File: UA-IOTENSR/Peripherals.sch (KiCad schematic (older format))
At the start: 3 parts, among them IC301 LM3914VX_NOPB, U301 SCD4X

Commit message: updated symbols; changed vdd to 3v3 global for pcb design later
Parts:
- DS1: renamed from DS301; symbol Samacs:HDSP-4832 -> UA-IOTENSR-rescue:HDSP-4832-Samacs
- IC1: renamed from IC301; symbol Samacs:LM3914VX_NOPB -> UA-IOTENSR-rescue:LM3914VX_NOPB-Samacs
- renumbered U301 to U4
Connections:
- net labels added: +3V3
- net labels removed: VDD
- wire segments 12 -> 35
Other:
- note added: "PERIPHERALS"
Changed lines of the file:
@@
 P 5750 1450
 AR Path="/61A2D97B" Ref="U?"  Part="1"
-AR Path="/61A1DC3C/61A2D97B" Ref="U301"  Part="1"
-F 0 "U301" H 5750 1915 50  0000 C CNN
+AR Path="/61A1DC3C/61A2D97B" Ref="U4"  Part="1"
+F 0 "U4" H 5750 1915 50  0000 C CNN
 F 1 "SCD4X" H 5750 1824 50  0000 C CNN
 F 2 "" H 5750 1900 50  0001 C CNN
@@
 P 5750 1950
 AR Path="/61A2D98B" Ref="#PWR?"  Part="1"
-AR Path="/61A1DC3C/61A2D98B" Ref="#PWR0302"  Part="1"
-F 0 "#PWR0302" H 5750 1700 50  0001 C CNN
+AR Path="/61A1DC3C/61A2D98B" Ref="#PWR022"  Part="1"
+F 0 "#PWR022" H 5750 1700 50  0001 C CNN
 F 1 "GND" H 5755 1777 50  0000 C CNN
 F 2 "" H 5750 1950 50  0001 C CNN
@@
 Wire Wire Line
 	5300 1400 5100 1400
-Text GLabel 5100 1400 0    50   Input ~ 0
-VDD
 Wire Wire Line
 	5300 1500 5300 1400
 Connection ~ 5300 1400
 $Comp
-L Samacs:HDSP-4832 DS?
+L UA-IOTENSR-rescue:HDSP-4832-Samacs DS?
 U 1 1 61A2D99B
-P 7400 4450
+P 7500 5300
 AR Path="/61A2D99B" Ref="DS?"  Part="1"
-AR Path="/61A1DC3C/61A2D99B" Ref="DS301"  Part="1"
-F 0 "DS301" H 8200 4715 50  0000 C CNN
-F 1 "HDSP-4832" H 8200 4624 50  0000 C CNN
-F 2 "DIPS762W61P254L2540H635Q20N" H 8850 4550 50  0001 L CNN
-F 3 "https://datasheet.datasheetarchive.com/originals/distributors/Datasheets-6/DSA-115790.pdf" H 8850 4450 50  0001 L CNN
-F 4 "Avago Light Bar Array Green/Red/Yellow LED Display, 1900 (Green) ??cd, 1900 (Yellow) ??cd, 3500 (Red) ??cd" H 8850 4350 50  0001 L CNN "Description"
-F 5 "6.35" H 8850 4250 50  0001 L CNN "Height"
-F 6 "630-HDSP-4832" H 8850 4150 50  0001 L CNN "Mouser Part Number"
-F 7 "https://www.mouser.co.uk/ProductDetail/Broadcom-Avago/HDSP-4832?qs=pQfy5%252BKCabLkjNEFwaYNQw%3D%3D" H 8850 4050 50  0001 L CNN "Mouser Price/Stock"
-F 8 "Avago Technologies" H 8850 3950 50  0001 L CNN "Manufacturer_Name"
-F 9 "HDSP-4832" H 8850 3850 50  0001 L CNN "Manufacturer_Part_Number"
-	1    7400 4450
+AR Path="/61A1DC3C/61A2D99B" Ref="DS1"  Part="1"
+F 0 "DS1" H 8300 5565 50  0000 C CNN
+F 1 "HDSP-4832" H 8300 5474 50  0000 C CNN
+F 2 "DIPS762W61P254L2540H635Q20N" H 8950 5400 50  0001 L CNN
+F 3 "https://datasheet.datasheetarchive.com/originals/distributors/Datasheets-6/DSA-115790.pdf" H 8950 5300 50  0001 L CNN
+F 4 "Avago Light Bar Array Green/Red/Yellow LED Display, 1900 (Green) ??cd, 1900 (Yellow) ??cd, 3500 (Red) ??cd" H 8950 5200 50  0001 L CNN "Description"
+F 5 "6.35" H 8950 5100 50  0001 L CNN "Height"
+F 6 "630-HDSP-4832" H 8950 5000 50  0001 L CNN "Mouser Part Number"
+F 7 "https://www.mouser.co.uk/ProductDetail/Broadcom-Avago/HDSP-4832?qs=pQfy5%252BKCabLkjNEFwaYNQw%3D%3D" H 8950 4900 50  0001 L CNN "Mouser Price/Stock"
+F 8 "Avago Technologies" H 8950 4800 50  0001 L CNN "Manufacturer_Name"
+F 9 "HDSP-4832" H 8950 4700 50  0001 L CNN "Manufacturer_Part_Number"
+	1    7500 5300
+	-1   0    0    1
+$EndComp
+Wire Wire Line
+	3000 4650 2800 4650
+$Comp
+L power:GND #PWR?
+U 1 1 61A2D9AF
+P 4100 3650
+AR Path="/61A2D9AF" Ref="#PWR?"  Part="1"
+AR Path="/61A1DC3C/61A2D9AF" Ref="#PWR021"  Part="1"
+F 0 "#PWR021" H 4100 3400 50  0001 C CNN
+F 1 "GND" H 4105 3477 50  0000 C CNN
+F 2 "" H 4100 3650 50  0001 C CNN
+F 3 "" H 4100 3650 50  0001 C CNN
+	1    4100 3650
+	-1   0    0    1
+$EndComp
+NoConn ~ 3000 5250
+Text Notes 7050 7000 0    236  ~ 0
+PERIPHERALS
+Wire Wire Line
+	5000 4400 5900 4400
+Wire Wire Line
+	5000 4500 5900 4500
+Wire Wire Line
+	5000 4600 5900 4600
+Wire Wire Line
+	5000 4700 5900 4700
+Wire Wire Line
+	5000 4800 5900 4800
+Wire Wire Line
+	5000 4900 5900 4900
+Wire Wire Line
+	5000 5000 5900 5000
+Wire Wire Line
+	5000 5100 5900 5100
+Wire Wire Line
+	5900 5200 5000 5200
+Wire Wire Line
+	5000 5300 5900 5300
+Wire Wire Line
+	7500 5300 7500 5200
+Connection ~ 7500 4500
+Wire Wire Line
+	7500 4500 7500 4400
+Connection ~ 7500 4600
+Wire Wire Line
+	7500 4600 7500 4500
+Connection ~ 7500 4700
+Wire Wire Line
+	7500 4700 7500 4600
+Connection ~ 7500 4800
+Wire Wire Line
+	7500 4800 7500 4700
+Connection ~ 7500 4900
+Wire Wire Line
+	7500 4900 7500 4800
+Connection ~ 7500 5000
+Wire Wire Line
+	7500 5000 7500 4900
+Connection ~ 7500 5100
+Wire Wire Line
+	7500 5100 7500 5000
+Connection ~ 7500 5200
+Wire Wire Line
+	7500 5200 7500 5100
+Wire Wire Line
+	7500 4400 7500 4150
+Connection ~ 7500 4400
+Wire Wire Line
+	3900 3850 3900 3700
+Wire Wire Line
+	4100 3850 4100 3650
+Wire Wire Line
+	4000 3850 4000 3700
+Wire Wire Line
+	4000 3700 3900 3700
+Connection ~ 3900 3700
+Wire Wire Line
+	3900 3700 3900 3650
+NoConn ~ 3000 5150
+$Comp
+L power:+3V3 #PWR?
+U 1 1 61A1C945
+P 5100 1400
+F 0 "#PWR?" H 5100 1250 50  0001 C CNN
+F 1 "+3V3" H 5115 1573 50  0000 C CNN
+F 2 "" H 5100 1400 50  0001 C CNN
+F 3 "" H 5100 1400 50  0001 C CNN
+	1    5100 1400
 	1    0    0    -1
 $EndComp
 $Comp
-L Samacs:LM3914VX_NOPB IC?
-U 1 1 61A2D9A7
-P 2750 4600
-AR Path="/61A2D9A7" Ref="IC?"  Part="1"
-AR Path="/61A1DC3C/61A2D9A7" Ref="IC301"  Part="1"
-F 0 "IC301" H 4794 4296 50  0000 L CNN
-F 1 "LM3914VX_NOPB" H 4794 4205 50  0000 L CNN
-F 2 "PLCC127P990X990X457-20N" H 4600 5100 50  0001 L CNN
-F 3 "http://www.ti.com/lit/gpn/lm3914" H 4600 5000 50  0001 L CNN
-F 4 "Dot/Bar Display Driver" H 4600 4900 50  0001 L CNN "Description"
-F 5 "4.57" H 4600 4800 50  0001 L CNN "Height"
-F 6 "926-LM3914VX/NOPB" H 4600 4700 50  0001 L CNN "Mouser Part Number"
-F 7 "https://www.mouser.co.uk/ProductDetail/Texas-Instruments/LM3914VX-NOPB?qs=QbsRYf82W3FGYq5LQoAqbA%3D%3D" H 4600 4600 50  0001 L CNN "Mouser Price/Stock"
-F 8 "Texas Instruments" H 4600 4500 50  0001 L CNN "Manufacturer_Name"
-F 9 "LM3914VX/NOPB" H 4600 4400 50  0001 L CNN "Manufacturer_Part_Number"
-	1    2750 4600
+L power:+3V3 #PWR?
+U 1 1 61A1E13D
+P 3900 3650
+F 0 "#PWR?" H 3900 3500 50  0001 C CNN
+F 1 "+3V3" H 3915 3823 50  0000 C CNN
+F 2 "" H 3900 3650 50  0001 C CNN
+F 3 "" H 3900 3650 50  0001 C CNN
+	1    3900 3650
 	1    0    0    -1
 $EndComp
-NoConn ~ 3550 6000
-NoConn ~ 2750 4900
 $Comp
-L power:GND #PWR?
-U 1 1 61A2D9AF
-P 3650 3700
-AR Path="/61A2D9AF" Ref="#PWR?"  Part="1"
-AR Path="/61A1DC3C/61A2D9AF" Ref="#PWR0301"  Part="1"
-F 0 "#PWR0301" H 3650 3450 50  0001 C CNN
-F 1 "GND" H 3655 3527 50  0000 C CNN
-F 2 "" H 3650 3700 50  0001 C CNN
-F 3 "" H 3650 3700 50  0001 C CNN
-	1    3650 3700
-	-1   0    0    1
+L power:+3V3 #PWR?
+U 1 1 61A1F555
+P 7500 4150
+F 0 "#PWR?" H 7500 4000 50  0001 C CNN
+F 1 "+3V3" H 7515 4323 50  0000 C CNN
+F 2 "" H 7500 4150 50  0001 C CNN
+F 3 "" H 7500 4150 50  0001 C CNN
+	1    7500 4150
+	1    0    0    -1
 $EndComp
-Wire Wire Line
-	3650 3900 3650 3700
-Wire Wire Line
-	3550 3900 3550 3800
-Text GLabel 3550 3800 0    50   Input ~ 0
-VDD
-Wire Wire Line
-	2750 4700 2550 4700
+$Comp
+L UA-IOTENSR-rescue:LM3914VX_NOPB-Samacs IC?
+U 1 1 61A2D9A7
+P 3000 4550
+AR Path="/61A2D9A7" Ref="IC?"  Part="1"
+AR Path="/61A1DC3C/61A2D9A7" Ref="IC1"  Part="1"
+F 0 "IC1" H 3250 3300 50  0000 C CNN
+F 1 "LM3914VX_NOPB" H 3500 3200 50  0000 C CNN
+F 2 "PLCC127P990X990X457-20N" H 4850 5050 50  0001 L CNN
+F 3 "http://www.ti.com/lit/gpn/lm3914" H 4850 4950 50  0001 L CNN
+F 4 "Dot/Bar Display Driver" H 4850 4850 50  0001 L CNN "Description"
+F 5 "4.57" H 4850 4750 50  0001 L CNN "Height"
+F 6 "926-LM3914VX/NOPB" H 4850 4650 50  0001 L CNN "Mouser Part Number"
+F 7 "https://www.mouser.co.uk/ProductDetail/Texas-Instruments/LM3914VX-NOPB?qs=QbsRYf82W3FGYq5LQoAqbA%3D%3D" H 4850 4550 50  0001 L CNN "Mouser Price/Stock"
+F 8 "Texas Instruments" H 4850 4450 50  0001 L CNN "Manufacturer_Name"
+F 9 "LM3914VX/NOPB" H 4850 4350 50  0001 L CNN "Manufacturer_Part_Number"
+	1    3000 4550
+	1    0    0    -1
+$EndComp
 $EndSCHEMATC

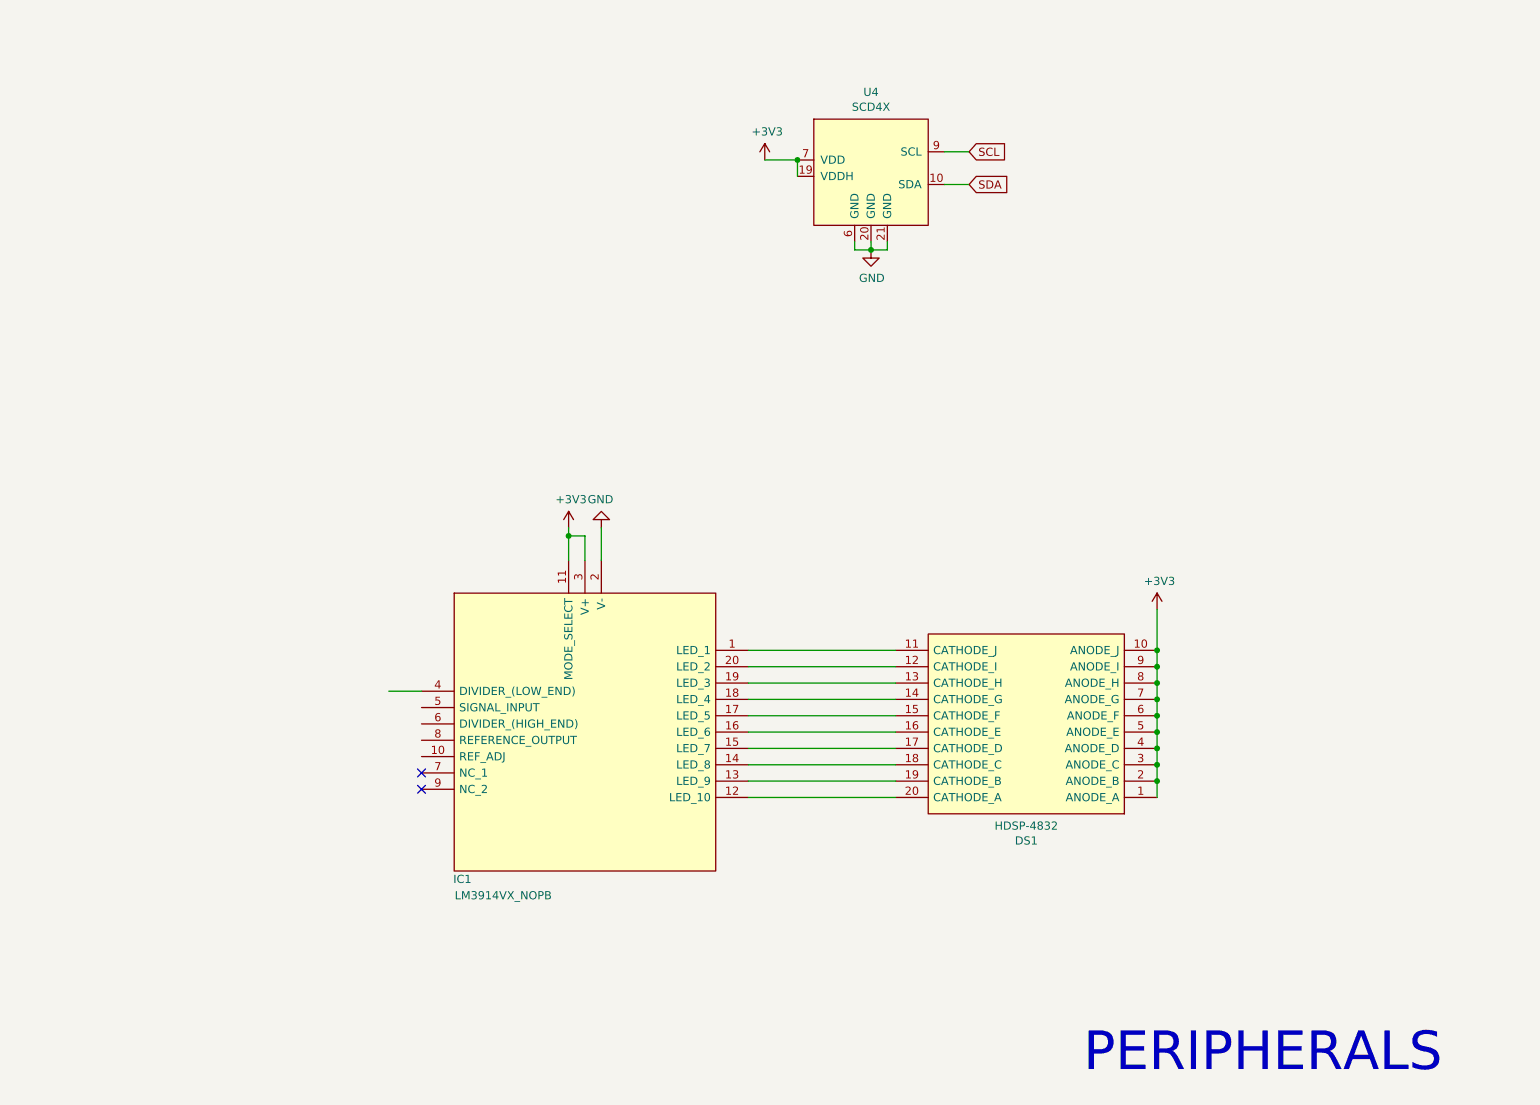
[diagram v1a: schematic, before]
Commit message: Finished LED bar graph array schem
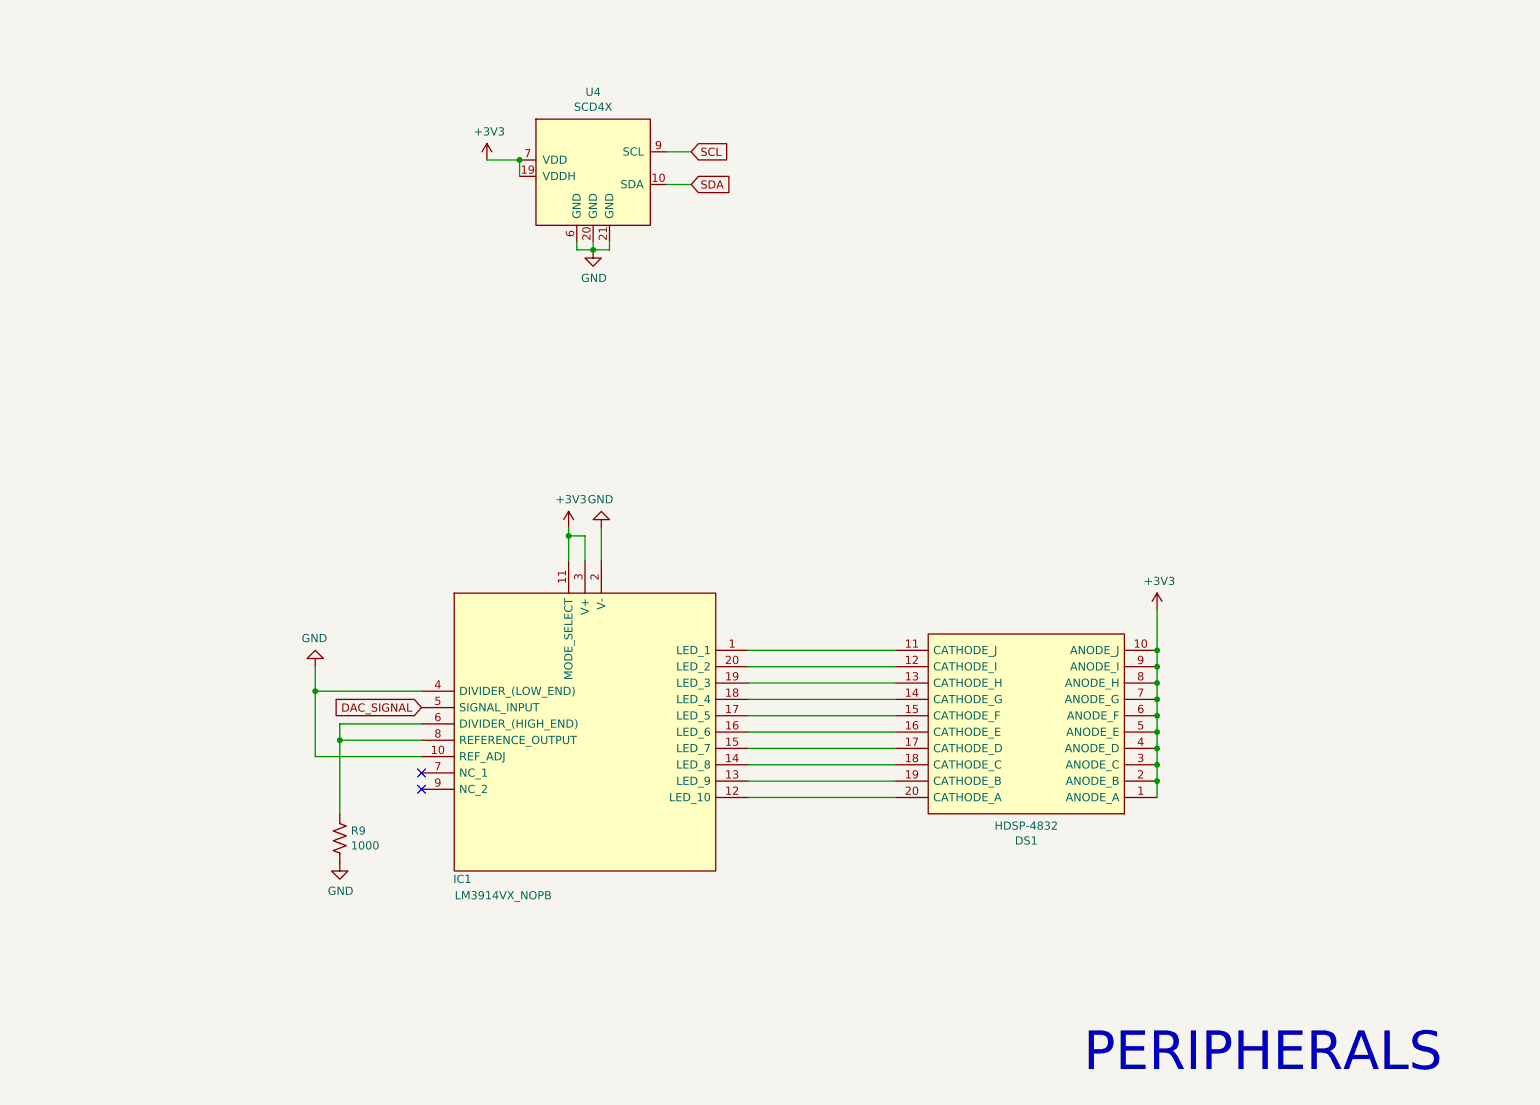
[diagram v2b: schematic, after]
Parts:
- added R9: 1000, symbol Device:R_US
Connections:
- net GND: now also IC1.10 (REF_ADJ), IC1.4 (DIVIDER_(LOW_END)), R9.2
- net DAC_SIGNAL: now reaches IC1.5 (SIGNAL_INPUT)
- net at IC1.6 (DIVIDER_(HIGH_END)): now also IC1.8 (REFERENCE_OUTPUT), R9.1
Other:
- moved on the sheet: U4
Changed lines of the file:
@@
 L SCD4X:SCD4X U?
 U 1 1 61A2D97B
-P 5750 1450
+P 4050 1450
 AR Path="/61A2D97B" Ref="U?"  Part="1"
 AR Path="/61A1DC3C/61A2D97B" Ref="U4"  Part="1"
-F 0 "U4" H 5750 1915 50  0000 C CNN
-F 1 "SCD4X" H 5750 1824 50  0000 C CNN
-F 2 "" H 5750 1900 50  0001 C CNN
-F 3 "" H 5750 1900 50  0001 C CNN
-	1    5750 1450
-	1    0    0    -1
-$EndComp
-Wire Wire Line
-	6200 1350 6350 1350
-Wire Wire Line
-	6200 1550 6350 1550
-Text GLabel 6350 1350 2    50   Input ~ 0
+F 0 "U4" H 4050 1915 50  0000 C CNN
+F 1 "SCD4X" H 4050 1824 50  0000 C CNN
+F 2 "" H 4050 1900 50  0001 C CNN
+F 3 "" H 4050 1900 50  0001 C CNN
+	1    4050 1450
+	1    0    0    -1
+$EndComp
+Wire Wire Line
+	4500 1350 4650 1350
+Wire Wire Line
+	4500 1550 4650 1550
+Text GLabel 4650 1350 2    50   Input ~ 0
 SCL
-Text GLabel 6350 1550 2    50   Input ~ 0
+Text GLabel 4650 1550 2    50   Input ~ 0
 SDA
 Wire Wire Line
-	5650 1900 5650 1950
-Wire Wire Line
-	5650 1950 5750 1950
-Wire Wire Line
-	5850 1950 5850 1900
-Wire Wire Line
-	5750 1900 5750 1950
-Connection ~ 5750 1950
-Wire Wire Line
-	5750 1950 5850 1950
+	3950 1900 3950 1950
+Wire Wire Line
+	3950 1950 4050 1950
+Wire Wire Line
+	4150 1950 4150 1900
+Wire Wire Line
+	4050 1900 4050 1950
+Connection ~ 4050 1950
+Wire Wire Line
+	4050 1950 4150 1950
 $Comp
 L power:GND #PWR?
 U 1 1 61A2D98B
-P 5750 1950
+P 4050 1950
 AR Path="/61A2D98B" Ref="#PWR?"  Part="1"
 AR Path="/61A1DC3C/61A2D98B" Ref="#PWR022"  Part="1"
-F 0 "#PWR022" H 5750 1700 50  0001 C CNN
-F 1 "GND" H 5755 1777 50  0000 C CNN
-F 2 "" H 5750 1950 50  0001 C CNN
-F 3 "" H 5750 1950 50  0001 C CNN
-	1    5750 1950
-	1    0    0    -1
-$EndComp
-Wire Wire Line
-	5300 1400 5100 1400
-Wire Wire Line
-	5300 1500 5300 1400
-Connection ~ 5300 1400
+F 0 "#PWR022" H 4050 1700 50  0001 C CNN
+F 1 "GND" H 4055 1777 50  0000 C CNN
+F 2 "" H 4050 1950 50  0001 C CNN
+F 3 "" H 4050 1950 50  0001 C CNN
+	1    4050 1950
+	1    0    0    -1
+$EndComp
+Wire Wire Line
+	3600 1400 3400 1400
+Wire Wire Line
+	3600 1500 3600 1400
+Connection ~ 3600 1400
 $Comp
 L UA-IOTENSR-rescue:HDSP-4832-Samacs DS?
@@
 	-1   0    0    1
 $EndComp
-Wire Wire Line
-	3000 4650 2800 4650
 $Comp
 L power:GND #PWR?
@@
 NoConn ~ 3000 5150
 $Comp
-L power:+3V3 #PWR?
+L power:+3V3 #PWR029
 U 1 1 61A1C945
-P 5100 1400
-F 0 "#PWR?" H 5100 1250 50  0001 C CNN
-F 1 "+3V3" H 5115 1573 50  0000 C CNN
-F 2 "" H 5100 1400 50  0001 C CNN
-F 3 "" H 5100 1400 50  0001 C CNN
-	1    5100 1400
-	1    0    0    -1
-$EndComp
-$Comp
-L power:+3V3 #PWR?
+P 3400 1400
+F 0 "#PWR029" H 3400 1250 50  0001 C CNN
+F 1 "+3V3" H 3415 1573 50  0000 C CNN
+F 2 "" H 3400 1400 50  0001 C CNN
+F 3 "" H 3400 1400 50  0001 C CNN
+	1    3400 1400
+	1    0    0    -1
+$EndComp
+$Comp
+L power:+3V3 #PWR028
 U 1 1 61A1E13D
 P 3900 3650
-F 0 "#PWR?" H 3900 3500 50  0001 C CNN
+F 0 "#PWR028" H 3900 3500 50  0001 C CNN
 F 1 "+3V3" H 3915 3823 50  0000 C CNN
 F 2 "" H 3900 3650 50  0001 C CNN
@@
 $EndComp
 $Comp
-L power:+3V3 #PWR?
+L power:+3V3 #PWR030
 U 1 1 61A1F555
 P 7500 4150
-F 0 "#PWR?" H 7500 4000 50  0001 C CNN
+F 0 "#PWR030" H 7500 4000 50  0001 C CNN
 F 1 "+3V3" H 7515 4323 50  0000 C CNN
 F 2 "" H 7500 4150 50  0001 C CNN
@@
 	1    0    0    -1
 $EndComp
+Text GLabel 3000 4750 0    50   Input ~ 0
+DAC_SIGNAL
+$Comp
+L power:GND #PWR026
+U 1 1 619D6C8A
+P 2350 4500
+F 0 "#PWR026" H 2350 4250 50  0001 C CNN
+F 1 "GND" H 2355 4327 50  0000 C CNN
+F 2 "" H 2350 4500 50  0001 C CNN
+F 3 "" H 2350 4500 50  0001 C CNN
+	1    2350 4500
+	-1   0    0    1
+$EndComp
+Wire Wire Line
+	3000 5050 2350 5050
+Wire Wire Line
+	2350 5050 2350 4650
+Wire Wire Line
+	2350 4650 3000 4650
+Connection ~ 2350 4650
+Wire Wire Line
+	2350 4650 2350 4500
+Wire Wire Line
+	3000 4950 2500 4950
+Wire Wire Line
+	3000 4850 2500 4850
+Wire Wire Line
+	2500 4850 2500 4950
+$Comp
+L Device:R_US R9
+U 1 1 619DD519
+P 2500 5550
+F 0 "R9" H 2568 5596 50  0000 L CNN
+F 1 "1000" H 2568 5505 50  0000 L CNN
+F 2 "" V 2540 5540 50  0001 C CNN
+F 3 "~" H 2500 5550 50  0001 C CNN
+	1    2500 5550
+	1    0    0    -1
+$EndComp
+$Comp
+L power:GND #PWR027
+U 1 1 619DE651
+P 2500 5700
+F 0 "#PWR027" H 2500 5450 50  0001 C CNN
+F 1 "GND" H 2505 5527 50  0000 C CNN
+F 2 "" H 2500 5700 50  0001 C CNN
+F 3 "" H 2500 5700 50  0001 C CNN
+	1    2500 5700
+	1    0    0    -1
+$EndComp
+Wire Wire Line
+	2500 4950 2500 5400
+Connection ~ 2500 4950
 $EndSCHEMATC
